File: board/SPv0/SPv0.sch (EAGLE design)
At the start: 19 parts, among them IC1 S34ML0XG1, IC2 F55[0/1]X---PT48, Q1 12MHz

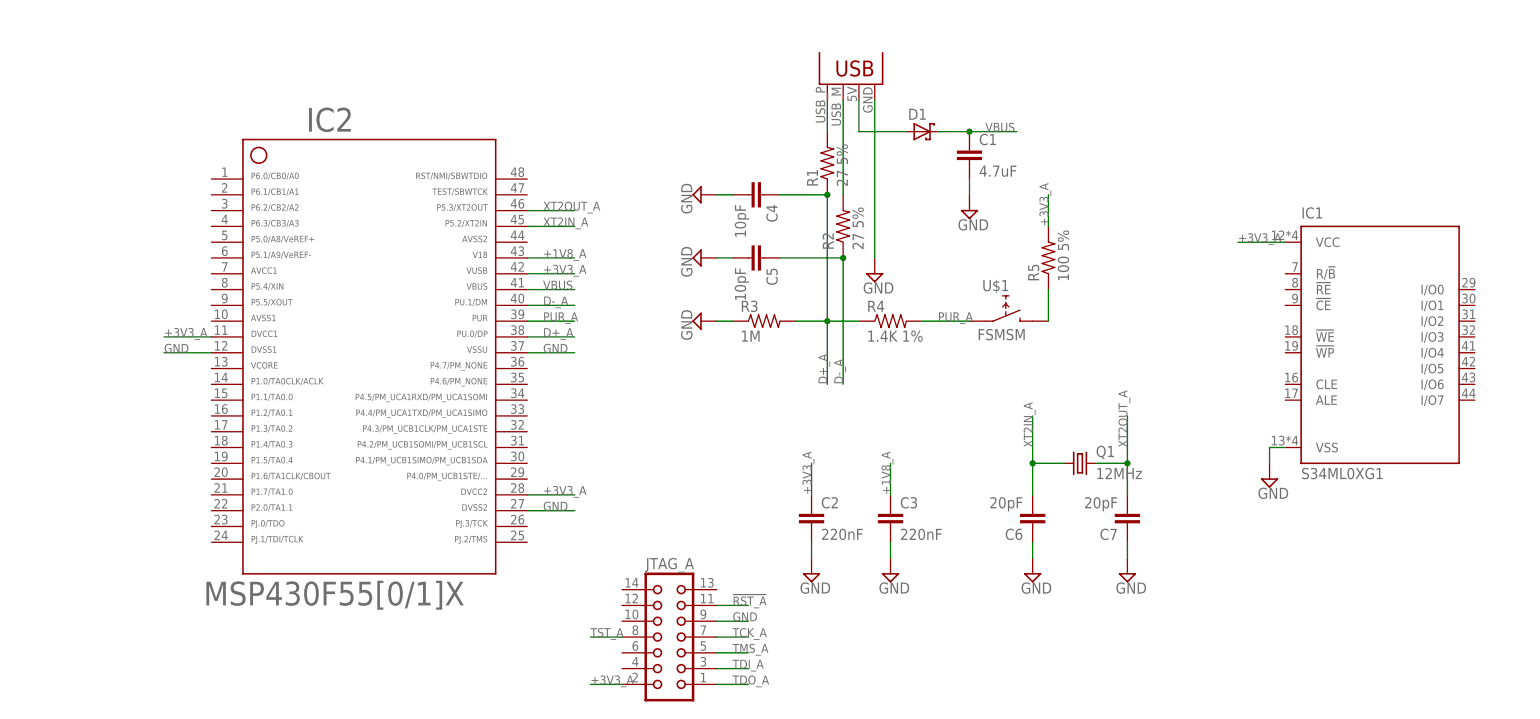
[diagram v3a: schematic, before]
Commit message: Added nets and busses for NAND/MSP430 interconnect Designated some pins for RNG
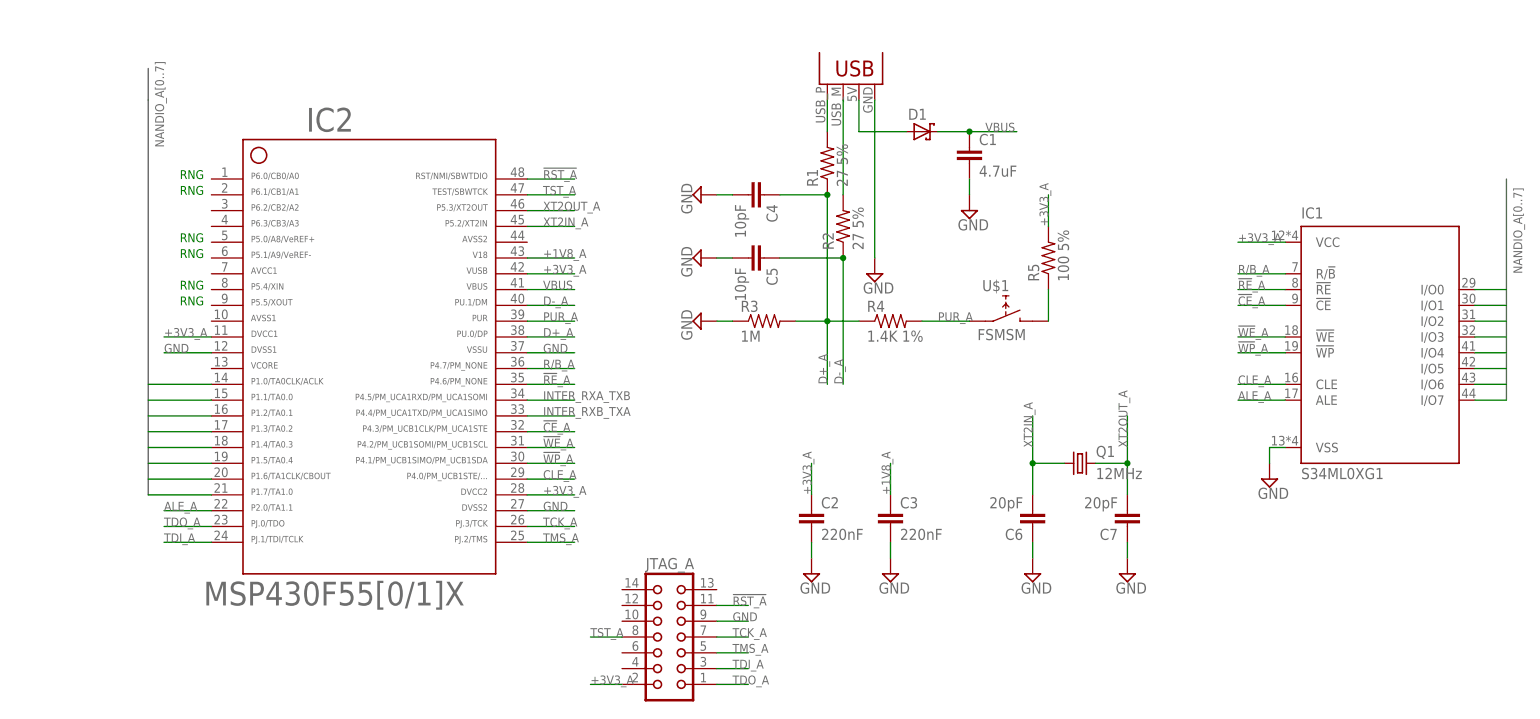
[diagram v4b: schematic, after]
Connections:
- new net !CE!_A: IC1.!CE, IC2.32
- new net !RE!_A: IC1.!RE, IC2.35
- new net !WE!_A: IC1.!WE, IC2.31
- new net !WP!_A: IC1.!WP, IC2.30
- new net ALE_A: IC1.ALE, IC2.22
- new net CLE_A: IC1.CLE, IC2.29
- new net INTER_RXA_TXB: IC2.34
- new net INTER_RXB_TXA: IC2.33
- new net NANDIO_A0: IC1.I/O0, IC2.14
- new net NANDIO_A1: IC1.I/O1, IC2.15
- new net NANDIO_A2: IC1.I/O2, IC2.16
- new net NANDIO_A3: IC1.I/O3, IC2.17
- new net NANDIO_A4: IC1.I/O4, IC2.18
- new net NANDIO_A5: IC1.I/O5, IC2.19
- new net NANDIO_A6: IC1.I/O6, IC2.20
- new net NANDIO_A7: IC1.I/O7, IC2.21
- new net R/B_A: IC1.R/!B, IC2.36
- net !RST_A!: now also IC2.48
- net TCK_A: now also IC2.26
- net TDI_A: now also IC2.24
- net TDO_A: now also IC2.23
- net TMS_A: now also IC2.25
- net TST_A: now also IC2.47
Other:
- note added: "RNG"
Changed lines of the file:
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@@
 <sheet>
 <plain>
+<text x="17.78" y="99.06" size="1.4224" layer="91">RNG</text>
+<text x="17.78" y="96.52" size="1.4224" layer="91">RNG</text>
+<text x="17.78" y="106.68" size="1.4224" layer="91">RNG</text>
+<text x="17.78" y="104.14" size="1.4224" layer="91">RNG</text>
+<text x="17.78" y="116.84" size="1.4224" layer="91">RNG</text>
+<text x="17.78" y="114.3" size="1.4224" layer="91">RNG</text>
 </plain>
 <instances>
@@
 </instances>
 <busses>
+<bus name="NANDIO_A[0..7]">
+<segment>
+<wire x1="231.14" y1="116.84" x2="231.14" y2="81.28" width="0.762" layer="92"/>
+<label x="233.68" y="101.6" size="1.4224" layer="95" rot="R90"/>
+</segment>
+<segment>
+<wire x1="12.7" y1="66.04" x2="12.7" y2="129.54" width="0.762" layer="92"/>
+<wire x1="12.7" y1="129.54" x2="12.7" y2="134.62" width="0.762" layer="92"/>
+<label x="15.24" y="121.92" size="1.4224" layer="95" rot="R90"/>
+</segment>
+</bus>
 </busses>
 <nets>
@@
 <label x="106.68" y="35.56" size="1.4224" layer="95"/>
 </segment>
+<segment>
+<pinref part="IC2" gate="G$1" pin="23"/>
+<wire x1="22.86" y1="60.96" x2="15.24" y2="60.96" width="0.1524" layer="91"/>
+<label x="15.24" y="60.96" size="1.4224" layer="95"/>
+</segment>
 </net>
 <net name="TDI_A" class="0">
@@
 <label x="106.68" y="38.1" size="1.4224" layer="95"/>
 </segment>
+<segment>
+<pinref part="IC2" gate="G$1" pin="24"/>
+<wire x1="22.86" y1="58.42" x2="15.24" y2="58.42" width="0.1524" layer="91"/>
+<label x="15.24" y="58.42" size="1.4224" layer="95"/>
+</segment>
 </net>
 <net name="TMS_A" class="0">
@@
 <label x="106.68" y="40.64" size="1.4224" layer="95"/>
 </segment>
+<segment>
+<pinref part="IC2" gate="G$1" pin="25"/>
+<wire x1="73.66" y1="58.42" x2="81.28" y2="58.42" width="0.1524" layer="91"/>
+<label x="76.2" y="58.42" size="1.4224" layer="95"/>
+</segment>
 </net>
 <net name="TCK_A" class="0">
@@
 <label x="106.68" y="43.18" size="1.4224" layer="95"/>
 </segment>
+<segment>
+<pinref part="IC2" gate="G$1" pin="26"/>
+<wire x1="73.66" y1="60.96" x2="81.28" y2="60.96" width="0.1524" layer="91"/>
+<label x="76.2" y="60.96" size="1.4224" layer="95"/>
+</segment>
 </net>
 <net name="!RST_A!" class="0">
@@
 <label x="106.68" y="48.26" size="1.4224" layer="95"/>
 </segment>
+<segment>
+<pinref part="IC2" gate="G$1" pin="48"/>
+<wire x1="73.66" y1="116.84" x2="81.28" y2="116.84" width="0.1524" layer="91"/>
+<label x="76.2" y="116.84" size="1.4224" layer="95"/>
+</segment>
 </net>
 <net name="TST_A" class="0">
@@
 <label x="83.82" y="43.18" size="1.4224" layer="95"/>
 </segment>
-</net>
+<segment>
+<pinref part="IC2" gate="G$1" pin="47"/>
+<wire x1="73.66" y1="114.3" x2="81.28" y2="114.3" width="0.1524" layer="91"/>
+<label x="76.2" y="114.3" size="1.4224" layer="95"/>
+</segment>
+</net>
+<net name="NANDIO_A0" class="0">
+<segment>
+<pinref part="IC1" gate="G$1" pin="I/O0"/>
+<wire x1="231.14" y1="99.06" x2="226.06" y2="99.06" width="0.1524" layer="91"/>
+</segment>
+<segment>
+<pinref part="IC2" gate="G$1" pin="14"/>
+<wire x1="12.7" y1="83.82" x2="22.86" y2="83.82" width="0.1524" layer="91"/>
+</segment>
+</net>
+<net name="NANDIO_A1" class="0">
+<segment>
+<pinref part="IC1" gate="G$1" pin="I/O1"/>
+<wire x1="231.14" y1="96.52" x2="226.06" y2="96.52" width="0.1524" layer="91"/>
+</segment>
+<segment>
+<pinref part="IC2" gate="G$1" pin="15"/>
+<wire x1="12.7" y1="81.28" x2="22.86" y2="81.28" width="0.1524" layer="91"/>
+</segment>
+</net>
+<net name="NANDIO_A2" class="0">
+<segment>
+<pinref part="IC1" gate="G$1" pin="I/O2"/>
+<wire x1="231.14" y1="93.98" x2="226.06" y2="93.98" width="0.1524" layer="91"/>
+</segment>
+<segment>
+<pinref part="IC2" gate="G$1" pin="16"/>
+<wire x1="12.7" y1="78.74" x2="22.86" y2="78.74" width="0.1524" layer="91"/>
+</segment>
+</net>
+<net name="NANDIO_A3" class="0">
+<segment>
+<pinref part="IC1" gate="G$1" pin="I/O3"/>
+<wire x1="231.14" y1="91.44" x2="226.06" y2="91.44" width="0.1524" layer="91"/>
+</segment>
+<segment>
+<pinref part="IC2" gate="G$1" pin="17"/>
+<wire x1="12.7" y1="76.2" x2="22.86" y2="76.2" width="0.1524" layer="91"/>
+</segment>
+</net>
+<net name="NANDIO_A4" class="0">
+<segment>
+<pinref part="IC1" gate="G$1" pin="I/O4"/>
+<wire x1="231.14" y1="88.9" x2="226.06" y2="88.9" width="0.1524" layer="91"/>
+</segment>
+<segment>
+<pinref part="IC2" gate="G$1" pin="18"/>
+<wire x1="12.7" y1="73.66" x2="22.86" y2="73.66" width="0.1524" layer="91"/>
+</segment>
+</net>
+<net name="NANDIO_A5" class="0">
+<segment>
+<pinref part="IC1" gate="G$1" pin="I/O5"/>
+<wire x1="231.14" y1="86.36" x2="226.06" y2="86.36" width="0.1524" layer="91"/>
+</segment>
+<segment>
+<pinref part="IC2" gate="G$1" pin="19"/>
+<wire x1="12.7" y1="71.12" x2="22.86" y2="71.12" width="0.1524" layer="91"/>
+</segment>
+</net>
+<net name="NANDIO_A6" class="0">
+<segment>
+<pinref part="IC1" gate="G$1" pin="I/O6"/>
+<wire x1="231.14" y1="83.82" x2="226.06" y2="83.82" width="0.1524" layer="91"/>
+</segment>
+<segment>
+<pinref part="IC2" gate="G$1" pin="20"/>
+<wire x1="12.7" y1="68.58" x2="22.86" y2="68.58" width="0.1524" layer="91"/>
+</segment>
+</net>
+<net name="NANDIO_A7" class="0">
+<segment>
+<pinref part="IC1" gate="G$1" pin="I/O7"/>
+<wire x1="231.14" y1="81.28" x2="226.06" y2="81.28" width="0.1524" layer="91"/>
+</segment>
+<segment>
+<pinref part="IC2" gate="G$1" pin="21"/>
+<wire x1="12.7" y1="66.04" x2="22.86" y2="66.04" width="0.1524" layer="91"/>
+</segment>
+</net>
+<net name="INTER_RXA_TXB" class="0">
+<segment>
+<pinref part="IC2" gate="G$1" pin="34"/>
+<wire x1="73.66" y1="81.28" x2="81.28" y2="81.28" width="0.1524" layer="91"/>
+<label x="76.2" y="81.28" size="1.4224" layer="95"/>
+</segment>
+</net>
+<net name="INTER_RXB_TXA" class="0">
+<segment>
+<pinref part="IC2" gate="G$1" pin="33"/>
+<wire x1="73.66" y1="78.74" x2="81.28" y2="78.74" width="0.1524" layer="91"/>
+<label x="76.2" y="78.74" size="1.4224" layer="95"/>
+</segment>
+</net>
+<net name="R/B_A" class="0">
+<segment>
+<pinref part="IC2" gate="G$1" pin="36"/>
+<wire x1="73.66" y1="86.36" x2="81.28" y2="86.36" width="0.1524" layer="91"/>
+<label x="76.2" y="86.36" size="1.4224" layer="95"/>
+</segment>
+<segment>
+<pinref part="IC1" gate="G$1" pin="R/!B"/>
+<wire x1="195.58" y1="101.6" x2="187.96" y2="101.6" width="0.1524" layer="91"/>
+<label x="187.96" y="101.6" size="1.4224" layer="95"/>
+</segment>
+</net>
+<net name="!RE!_A" class="0">
+<segment>
+<pinref part="IC2" gate="G$1" pin="35"/>
+<wire x1="73.66" y1="83.82" x2="81.28" y2="83.82" width="0.1524" layer="91"/>
+<label x="76.2" y="83.82" size="1.4224" layer="95"/>
+</segment>
+<segment>
+<pinref part="IC1" gate="G$1" pin="!RE"/>
+<wire x1="195.58" y1="99.06" x2="187.96" y2="99.06" width="0.1524" layer="91"/>
+<label x="187.96" y="99.06" size="1.4224" layer="95"/>
+</segment>
+</net>
+<net name="!CE!_A" class="0">
+<segment>
+<pinref part="IC2" gate="G$1" pin="32"/>
+<wire x1="73.66" y1="76.2" x2="81.28" y2="76.2" width="0.1524" layer="91"/>
+<label x="76.2" y="76.2" size="1.4224" layer="95"/>
+</segment>
+<segment>
+<pinref part="IC1" gate="G$1" pin="!CE"/>
+<wire x1="195.58" y1="96.52" x2="187.96" y2="96.52" width="0.1524" layer="91"/>
+<label x="187.96" y="96.52" size="1.4224" layer="95"/>
+</segment>
+</net>
+<net name="!WE!_A" class="0">
+<segment>
+<pinref part="IC2" gate="G$1" pin="31"/>
+<wire x1="73.66" y1="73.66" x2="81.28" y2="73.66" width="0.1524" layer="91"/>
+<label x="76.2" y="73.66" size="1.4224" layer="95"/>
+</segment>
+<segment>
+<pinref part="IC1" gate="G$1" pin="!WE"/>
+<wire x1="195.58" y1="91.44" x2="187.96" y2="91.44" width="0.1524" layer="91"/>
+<label x="187.96" y="91.44" size="1.4224" layer="95"/>
+</segment>
+</net>
+<net name="!WP!_A" class="0">
+<segment>
+<pinref part="IC2" gate="G$1" pin="30"/>
+<wire x1="73.66" y1="71.12" x2="81.28" y2="71.12" width="0.1524" layer="91"/>
+<label x="76.2" y="71.12" size="1.4224" layer="95"/>
+</segment>
+<segment>
+<pinref part="IC1" gate="G$1" pin="!WP"/>
+<wire x1="195.58" y1="88.9" x2="187.96" y2="88.9" width="0.1524" layer="91"/>
+<label x="187.96" y="88.9" size="1.4224" layer="95"/>
+</segment>
+</net>
+<net name="CLE_A" class="0">
+<segment>
+<pinref part="IC2" gate="G$1" pin="29"/>
+<wire x1="73.66" y1="68.58" x2="81.28" y2="68.58" width="0.1524" layer="91"/>
+<label x="76.2" y="68.58" size="1.4224" layer="95"/>
+</segment>
+<segment>
+<pinref part="IC1" gate="G$1" pin="CLE"/>
+<wire x1="195.58" y1="83.82" x2="187.96" y2="83.82" width="0.1524" layer="91"/>
+<label x="187.96" y="83.82" size="1.4224" layer="95"/>
+</segment>
+</net>
+<net name="ALE_A" class="0">
+<segment>
+<pinref part="IC2" gate="G$1" pin="22"/>
+<wire x1="22.86" y1="63.5" x2="15.24" y2="63.5" width="0.1524" layer="91"/>
+<label x="15.24" y="63.5" size="1.4224" layer="95"/>
+</segment>
+<segment>
+<pinref part="IC1" gate="G$1" pin="ALE"/>
+<wire x1="195.58" y1="81.28" x2="187.96" y2="81.28" width="0.1524" layer="91"/>
+<label x="187.96" y="81.28" size="1.4224" layer="95"/>
+</segment>
+</net>

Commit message: going with the avalanche noise for v0 starting in on initial layout of board
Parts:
- added C10: 4.7u, rcl:C-EUC0805
- added C11: 120pF, rcl:C-EUC0603
- added C12: 4.7uF, rcl:C-EUC0805
- added C13: 2.2uF, rcl:C-EUC0603
- added C8, C9: 0.47u, rcl:C-EUC0805
- added D2, D3: (no value), zetex:DSOD323
- added D4: (no value), diode:DIODE-SOD123
- added IC3: LM339D, linear:LM339D
- added R10, R7: 1M, rcl:R-US_R0805
- added R11, R12: 100K, rcl:R-US_R0805
- added R13: 1.2K, rcl:R-US_R0805
- added R14, R15: 10K, rcl:R-US_R0805
- added R16, R17: 5K, rcl:R-US_R0805
- added R18: 51K, rcl:R-US_R0603
- added R19: 205K, rcl:R-US_R0603
- added R20: 13.3K, rcl:R-US_R0603
- added R6: 150K, rcl:R-US_R0805
- added R8: 12K, rcl:R-US_R0805
- added R9: 47K, rcl:R-US_R0805
- added T1, T2: n3904, transistor:MMBT3904LT1-NPN-SOT23-BEC
- added T3, T4, T5: n3906, transistor:MMBT3906LT1-PNP-SOT23-BEC
- added TP2: PTR1PAD1-13, testpad:PTR1PAD1-13
- added U$2: LM27313, rng:LM27313
- added U$3: 10uH, rng:CB2518
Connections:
- removed net N$3: D1.A, JP1.VBUS
- new net AOUT: IC3B.OUT, R9.2, T5.B
- new net DOUT_1: R16.1, R17.2, TP2.TP
- new net N$10: IC3B.-IN, R8.2, R9.1
- new net N$11: IC3B.+IN, R10.1
- new net N$12: C10.1, IC3C.+IN, R11.1, R12.2
- new net N$13: D3.C, R14.2, T3.B
- new net N$14: D2.C, D3.A
- new net N$15: R13.1, T3.E
- new net N$16: T3.C, T4.E, T5.E
- new net N$17: R15.2, T4.C
- new net N$18: R17.1, T5.C
- new net N$19: R18.2, U$2.!SHDN!
- new net N$20: D4.A, U$2.SW, U$3.P$2
- new net N$21: C11.2, R19.2, R20.1, U$2.FB
- new net N$5: C8.1, R6.1, T1.E, T2.C
- new net N$6: T1.B, T2.B
- new net N$7: C8.2, IC3A.+IN, R7.1
- new net N$8: C9.1, IC3A.-IN, IC3A.OUT
- new net N$9: C9.2, R8.1
- new net VCC: C13.2, D1.A, JP1.VBUS, R18.1, U$2.VIN, U$3.P$1
- new net VDD: C11.1, C12.1, D2.A, D4.C, IC3P.V+, R11.2, R13.2, R19.1, R6.2
- new net VREF: IC3C.-IN, IC3C.OUT, R10.2, R7.2, T4.B
- net GND: now also C10.2, C12.2, C13.1, IC3P.GND, R12.1, R14.1, R15.1, R16.2, R20.2, T2.E, U$2.GND
